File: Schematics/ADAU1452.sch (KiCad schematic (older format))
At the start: 97 parts, among them CN201 COAX, P201 CONN_2x1, P203 CONN_6X2, P204 CONN_6x1, SW202 SWITCH, U201 ADAU1452WBCPZ, U202 ADM13307-5ARZ, U203 25AA1024, X201 24M576

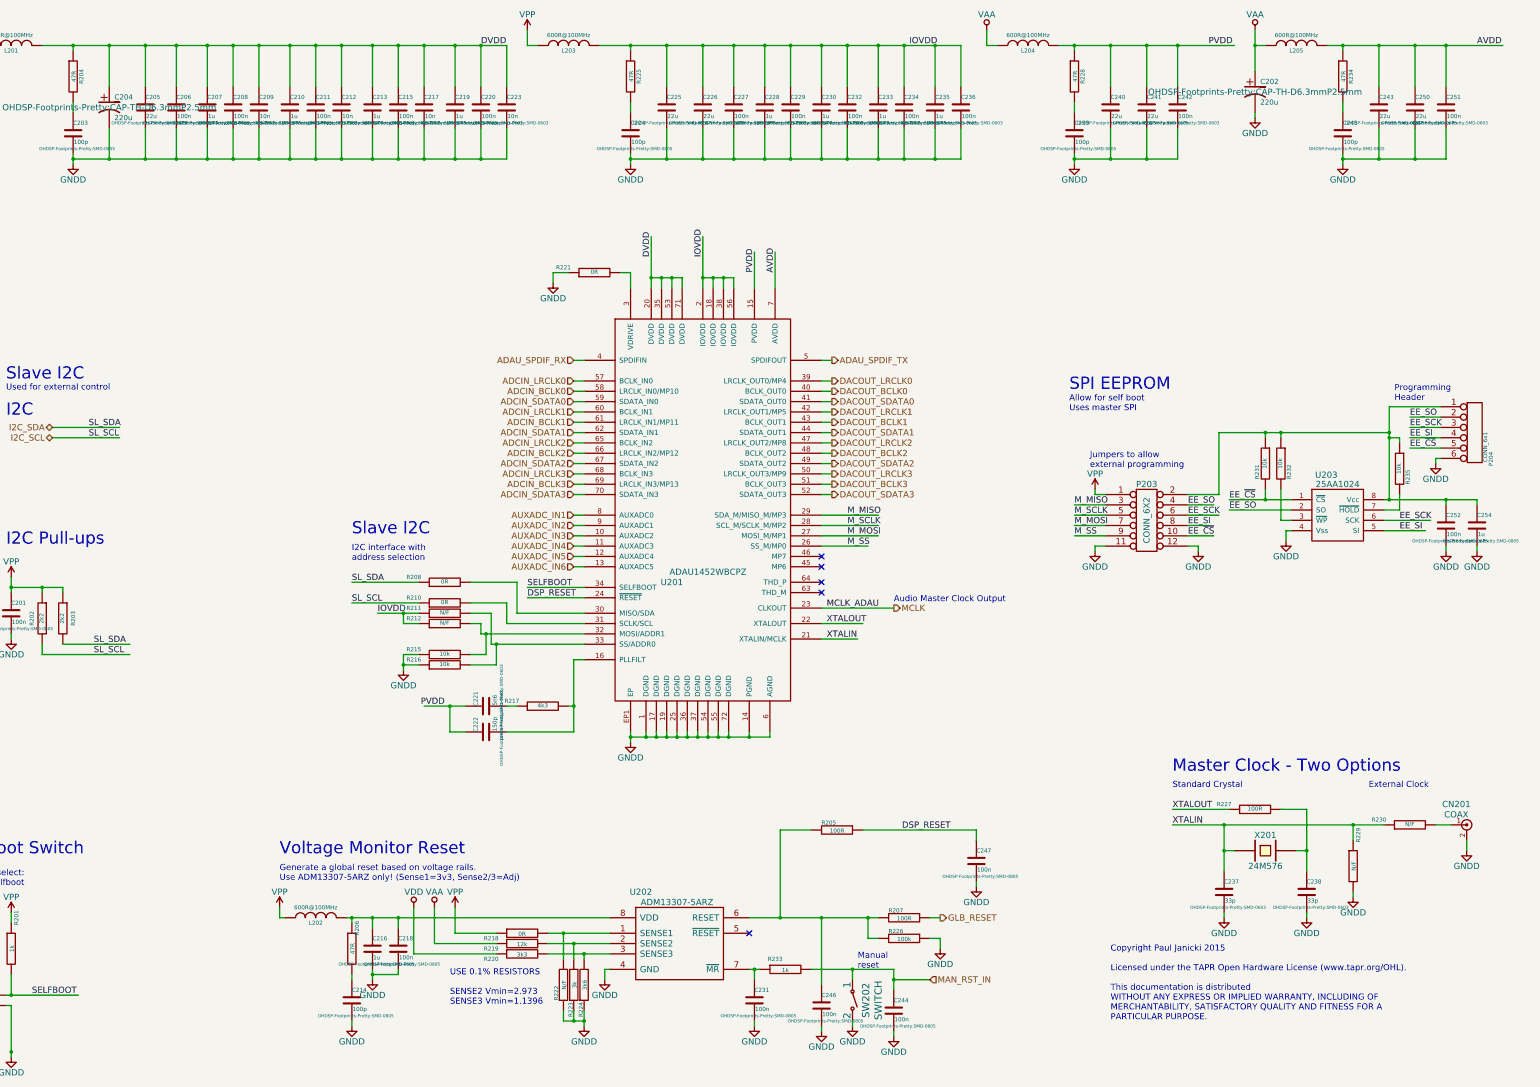
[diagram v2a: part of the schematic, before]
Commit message: WIP
Add master audio clock to I2S headers.
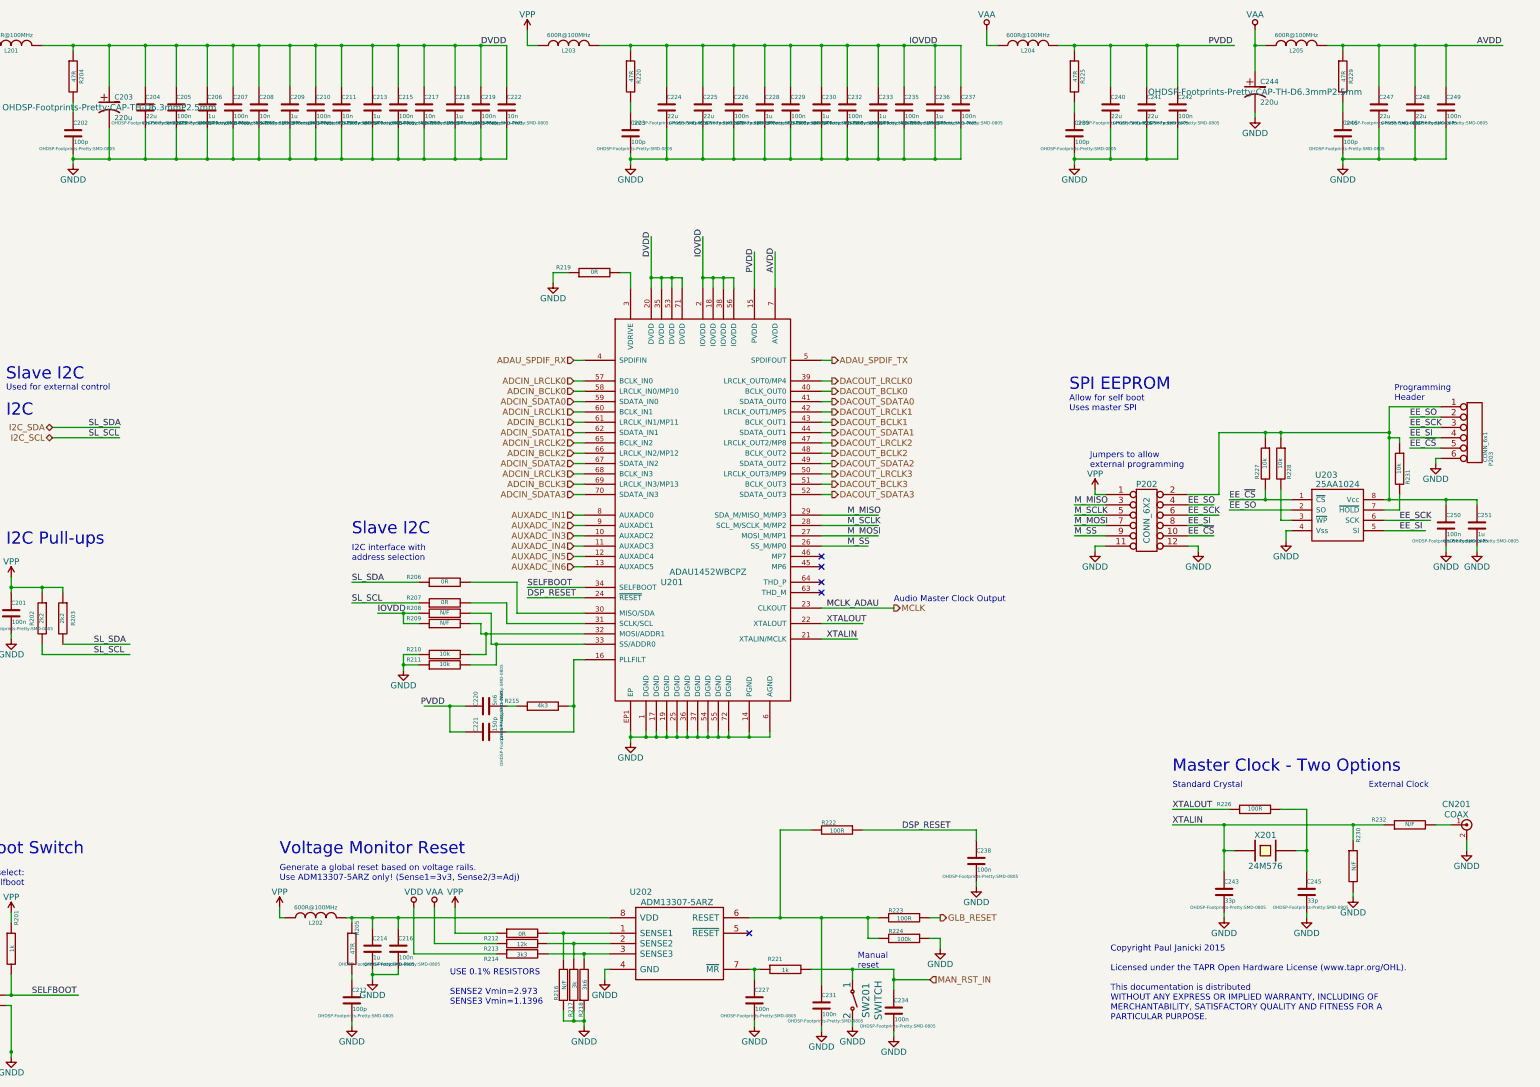
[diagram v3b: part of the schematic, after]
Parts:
- C206: renamed from C207; footprint OHDSP-Footprints-Pretty:SMD-0603 -> OHDSP-Footprints-Pretty:SMD-0805
- C207: renamed from C208; footprint OHDSP-Footprints-Pretty:SMD-0603 -> OHDSP-Footprints-Pretty:SMD-0805
- C208: renamed from C209; footprint OHDSP-Footprints-Pretty:SMD-0603 -> OHDSP-Footprints-Pretty:SMD-0805
- C209: renamed from C210; footprint OHDSP-Footprints-Pretty:SMD-0603 -> OHDSP-Footprints-Pretty:SMD-0805
- C210: renamed from C211; footprint OHDSP-Footprints-Pretty:SMD-0603 -> OHDSP-Footprints-Pretty:SMD-0805
- C211: renamed from C212; footprint OHDSP-Footprints-Pretty:SMD-0603 -> OHDSP-Footprints-Pretty:SMD-0805
- C213, C215, C217, C228, C229, C230, C232, C233, C242: footprint OHDSP-Footprints-Pretty:SMD-0603 -> OHDSP-Footprints-Pretty:SMD-0805
- C218: renamed from C219; footprint OHDSP-Footprints-Pretty:SMD-0603 -> OHDSP-Footprints-Pretty:SMD-0805
- C219: renamed from C220; footprint OHDSP-Footprints-Pretty:SMD-0603 -> OHDSP-Footprints-Pretty:SMD-0805
- C220: renamed from C221; footprint OHDSP-Footprints-Pretty:SMD-0603 -> OHDSP-Footprints-Pretty:SMD-0805
- C221: renamed from C222; footprint OHDSP-Footprints-Pretty:SMD-0603 -> OHDSP-Footprints-Pretty:SMD-0805
- C222: renamed from C223; footprint OHDSP-Footprints-Pretty:SMD-0603 -> OHDSP-Footprints-Pretty:SMD-0805
- C235: renamed from C234; footprint OHDSP-Footprints-Pretty:SMD-0603 -> OHDSP-Footprints-Pretty:SMD-0805
- C236: renamed from C235; footprint OHDSP-Footprints-Pretty:SMD-0603 -> OHDSP-Footprints-Pretty:SMD-0805
- C237: renamed from C236; footprint OHDSP-Footprints-Pretty:SMD-0603 -> OHDSP-Footprints-Pretty:SMD-0805
- C243: renamed from C237; footprint OHDSP-Footprints-Pretty:SMD-0603 -> OHDSP-Footprints-Pretty:SMD-0805
- C245: renamed from C238; footprint OHDSP-Footprints-Pretty:SMD-0603 -> OHDSP-Footprints-Pretty:SMD-0805
- C249: renamed from C251; footprint OHDSP-Footprints-Pretty:SMD-0603 -> OHDSP-Footprints-Pretty:SMD-0805
- R215: renamed from R217; footprint OHDSP-Footprints-Pretty:SMD-0603 -> OHDSP-Footprints-Pretty:SMD-0805
- renumbered C203 to C202, C204 to C203, C205 to C204, C206 to C205, C214 to C212, C216 to C214, C218 to C216, C224 to C223, C225 to C224, C226 to C225, C227 to C226, C231 to C227, C246 to C231, C244 to C234, C247 to C238, C202 to C244, C245 to C246, C243 to C247, C250 to C248, C252 to C250, C254 to C251, P203 to P202, P204 to P203, R206 to R205, R208 to R206, R210 to R207, R211 to R208, R212 to R209, R215 to R210, R216 to R211, R218 to R212, R219 to R213, R220 to R214, R222 to R216, R223 to R217, R224 to R218, R221 to R219, R225 to R220, R233 to R221, R205 to R222, R207 to R223, R226 to R224, R228 to R225, R227 to R226, R231 to R227, R232 to R228, R234 to R229, R229 to R230, R235 to R231, R230 to R232, SW202 to SW201

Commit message: WIP
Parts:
- added R233: N/F, OHDSP-Footprints-Pretty:SMD-0805, symbol R
- C206, C207, C208, C209, C210, C211, C213, C215, C217, C218, C219, C222, C228, C229, C230, C232, C233, C235, C236, C237: footprint OHDSP-Footprints-Pretty:SMD-0805 -> OHDSP-Footprints-Pretty:SMD-0603
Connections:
- wire segments 319 -> 321
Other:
- moved on the sheet: P202, R227

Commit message: WIP
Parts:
- C242, C249: footprint OHDSP-Footprints-Pretty:SMD-0805 -> OHDSP-Footprints-Pretty:SMD-0603
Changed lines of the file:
@@
 F 0 "C242" H 12500 1750 40  0000 L CNN
 F 1 "100n" H 12506 1565 40  0000 L CNN
-F 2 "OHDSP-Footprints-Pretty:SMD-0805" H 12538 1500 30  0000 C CNN
+F 2 "OHDSP-Footprints-Pretty:SMD-0603" H 12538 1500 30  0000 C CNN
 F 3 "~" H 12500 1650 60  0000 C CNN
 	1    12500 1650
@@
 F 0 "C249" H 15100 1750 40  0000 L CNN
 F 1 "100n" H 15106 1565 40  0000 L CNN
-F 2 "OHDSP-Footprints-Pretty:SMD-0805" H 15138 1500 30  0000 C CNN
+F 2 "OHDSP-Footprints-Pretty:SMD-0603" H 15138 1500 30  0000 C CNN
 F 3 "~" H 15100 1650 60  0000 C CNN
 	1    15100 1650

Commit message: WIP
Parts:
- removed C225, C241, C248: 22u, OHDSP-Footprints-Pretty:SMD-0805, symbol C
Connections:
- wire segments 321 -> 315
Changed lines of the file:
@@
-$EndComp
-$Comp
-L C C225
-U 1 1 54DB1F7E
-P 7900 1650
-F 0 "C225" H 7900 1750 40  0000 L CNN
-F 1 "22u" H 7906 1565 40  0000 L CNN
-F 2 "OHDSP-Footprints-Pretty:SMD-0805" H 7938 1500 30  0000 C CNN
-F 3 "~" H 7900 1650 60  0000 C CNN
-	1    7900 1650
-	1    0    0    -1
 $EndComp
 $Comp
@@
 	1    0    0    -1
 $EndComp
-$Comp
-L C C241
-U 1 1 54DB300D
-P 12200 1650
-F 0 "C241" H 12200 1750 40  0000 L CNN
-F 1 "22u" H 12206 1565 40  0000 L CNN
-F 2 "OHDSP-Footprints-Pretty:SMD-0805" H 12238 1500 30  0000 C CNN
-F 3 "~" H 12200 1650 60  0000 C CNN
-	1    12200 1650
-	1    0    0    -1
-$EndComp
 Text Label 12800 1050 0    60   ~ 0
 PVDD
@@
 F 3 "~" H 15100 1650 60  0000 C CNN
 	1    15100 1650
-	1    0    0    -1
-$EndComp
-$Comp
-L C C248
-U 1 1 54DB3C95
-P 14800 1650
-F 0 "C248" H 14800 1750 40  0000 L CNN
-F 1 "22u" H 14806 1565 40  0000 L CNN
-F 2 "OHDSP-Footprints-Pretty:SMD-0805" H 14838 1500 30  0000 C CNN
-F 3 "~" H 14800 1650 60  0000 C CNN
-	1    14800 1650
 	1    0    0    -1
 $EndComp
@@
 	7550 1050 7550 1450
 Connection ~ 7200 1050
-Wire Wire Line
-	7900 1050 7900 1450
 Connection ~ 7550 1050
-Connection ~ 7900 1050
 Wire Wire Line
 	7200 2100 7200 2200
@@
 	7550 2150 7550 1850
 Connection ~ 7200 2150
-Wire Wire Line
-	7900 2150 7900 1850
 Connection ~ 7550 2150
-Connection ~ 7900 2150
 Wire Wire Line
 	8200 1050 8200 1450
@@
 	11850 1050 11850 1450
 Connection ~ 11500 1050
-Wire Wire Line
-	12200 1050 12200 1450
 Connection ~ 11850 1050
-Connection ~ 12200 1050
 Wire Wire Line
 	11500 2100 11500 2200
@@
 	11850 2150 11850 1850
 Connection ~ 11500 2150
-Wire Wire Line
-	12200 2150 12200 1850
 Connection ~ 11850 2150
-Connection ~ 12200 2150
 Wire Wire Line
 	12500 1050 12500 1450
@@
 	14450 1050 14450 1450
 Connection ~ 14100 1050
-Wire Wire Line
-	14800 1050 14800 1450
 Connection ~ 14450 1050
-Connection ~ 14800 1050
 Wire Wire Line
 	14100 2100 14100 2200
@@
 	14450 2150 14450 1850
 Connection ~ 14100 2150
-Wire Wire Line
-	14800 2150 14800 1850
 Connection ~ 14450 2150
-Connection ~ 14800 2150
 Wire Wire Line
 	15100 1050 15100 1450

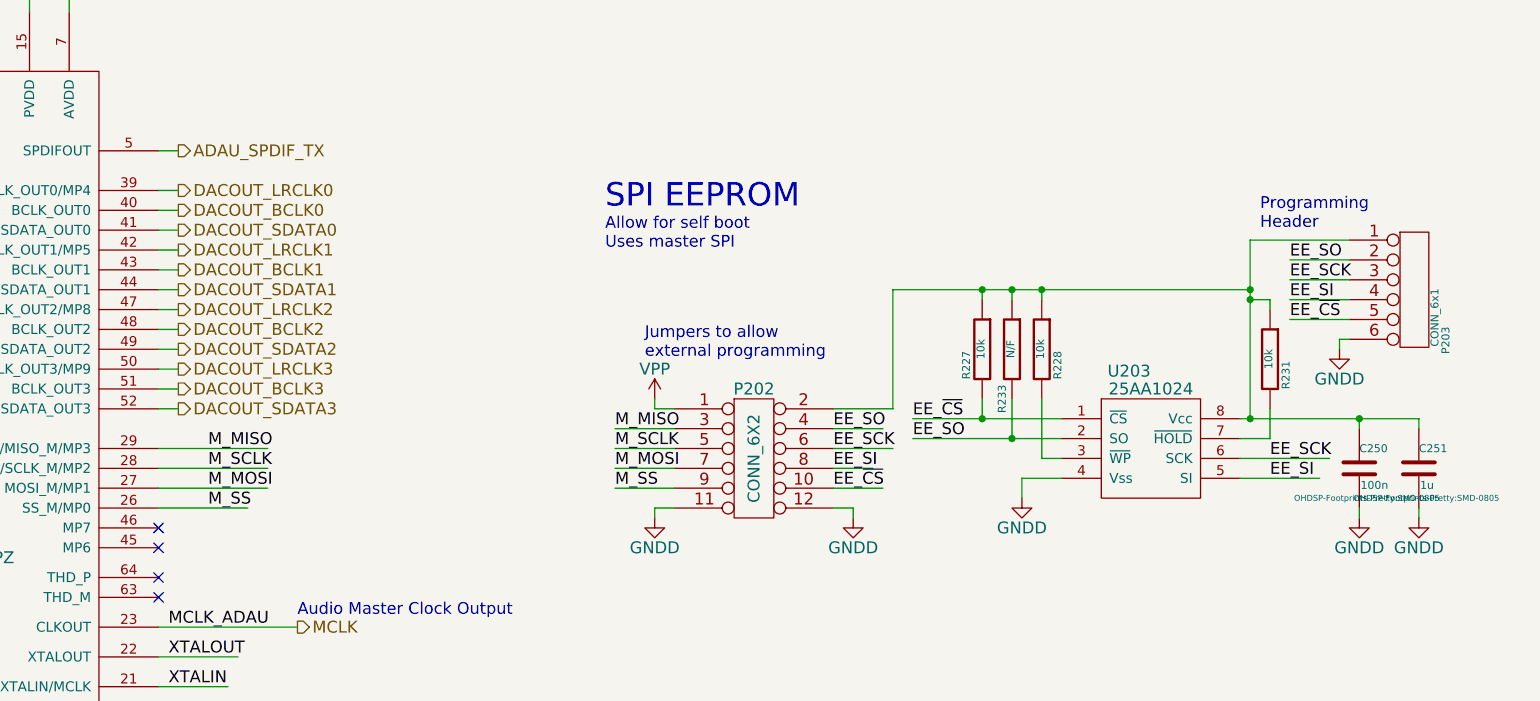
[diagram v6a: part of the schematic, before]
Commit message: WIP
Remove unneeded parts around SPI EEPROM
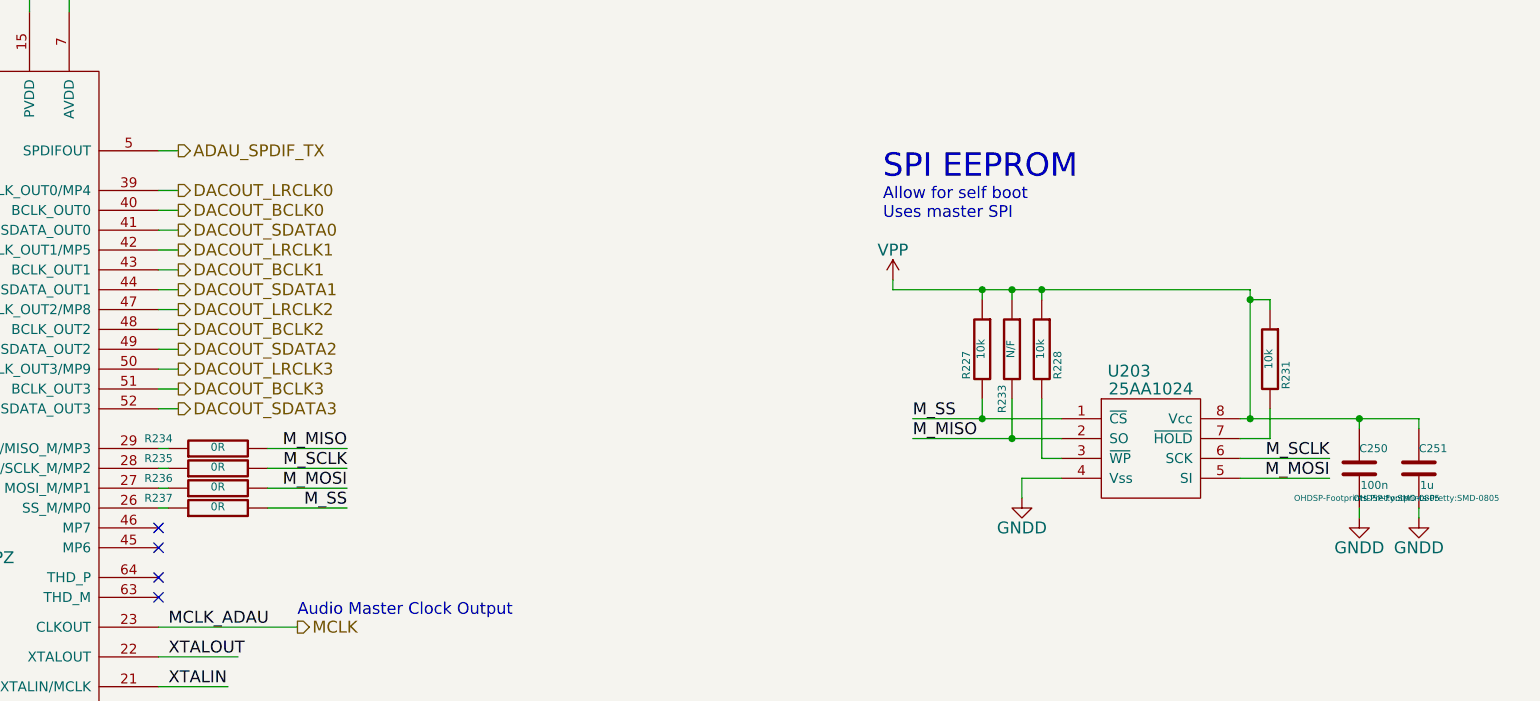
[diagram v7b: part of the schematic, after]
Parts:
- removed P202: CONN_6X2, OHDSP-Footprints-Pretty:CONN_DIL_2X6, symbol CONN_6X2
- removed P203: CONN_6x1, OHDSP-Footprints-Pretty:CONN_SIL_6, symbol CONN_6x1
- added R234, R235, R236, R237: 0R, OHDSP-Footprints-Pretty:SMD-0805, symbol R
- U203: footprint OHDSP-Footprints-Pretty:IC_SOIC_8 -> OHDSP-Footprints-Pretty:IC_DIP_8
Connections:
- net labels removed: EE_SCK, EE_SI, EE_SO, EE_~CS
- wire segments 315 -> 297
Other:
- note removed: "Jumpers to allow \nexternal programming\n"
- note removed: "Programming\nHeader\n"
